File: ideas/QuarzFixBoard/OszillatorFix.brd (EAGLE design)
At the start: 8.3 x 7 mm, 4 parts, among them Q2 ASF1

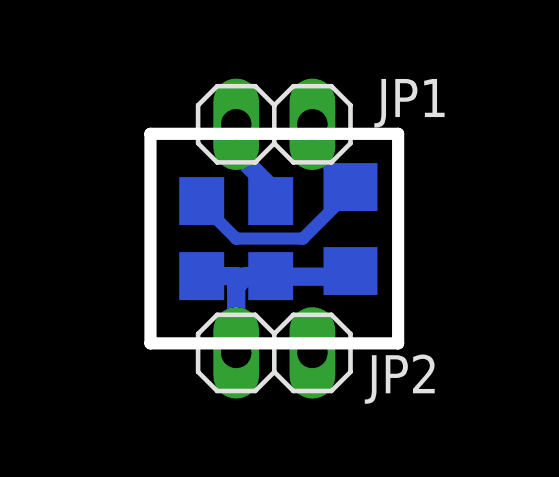
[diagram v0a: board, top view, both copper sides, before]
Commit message: New position for capacitor near to oscillator
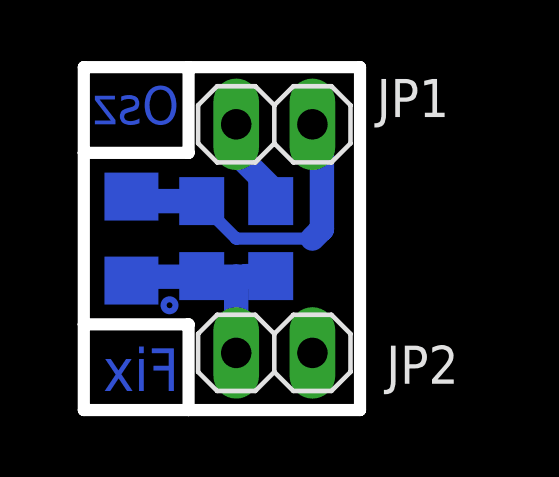
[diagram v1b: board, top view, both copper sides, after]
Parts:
- moved C7 7.31 mm to (-0.64, 3.49)
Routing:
- net GND2: track 8.36 -> 11.5 mm
- net VCC: track 9.77 -> 11.0 mm
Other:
- board size 8.3 x 7 mm -> 9.2 x 11.4 mm
- board text added: "Fix"
- board text added: "Osz"
